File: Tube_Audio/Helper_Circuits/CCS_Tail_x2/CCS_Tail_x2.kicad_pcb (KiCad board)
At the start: 2 copper layers, 67.3 x 45.7 mm, 15 parts, among them J1 Screw_Terminal_01x03, Q1 IXCP10M45S, Q2 IXCP10M45S

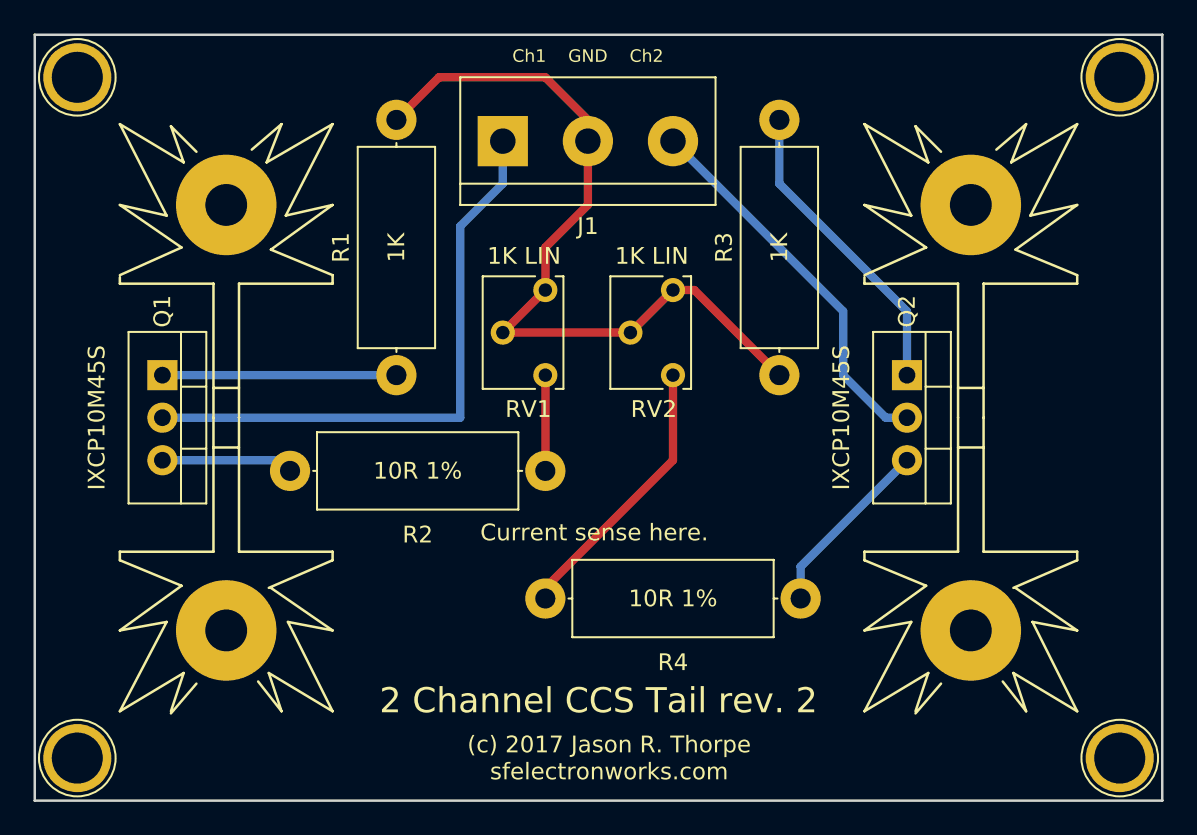
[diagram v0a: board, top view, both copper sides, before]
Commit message: Rev the CCS tail board -- use the Bourns 4-turn trim pots, and shrink the board a bit.
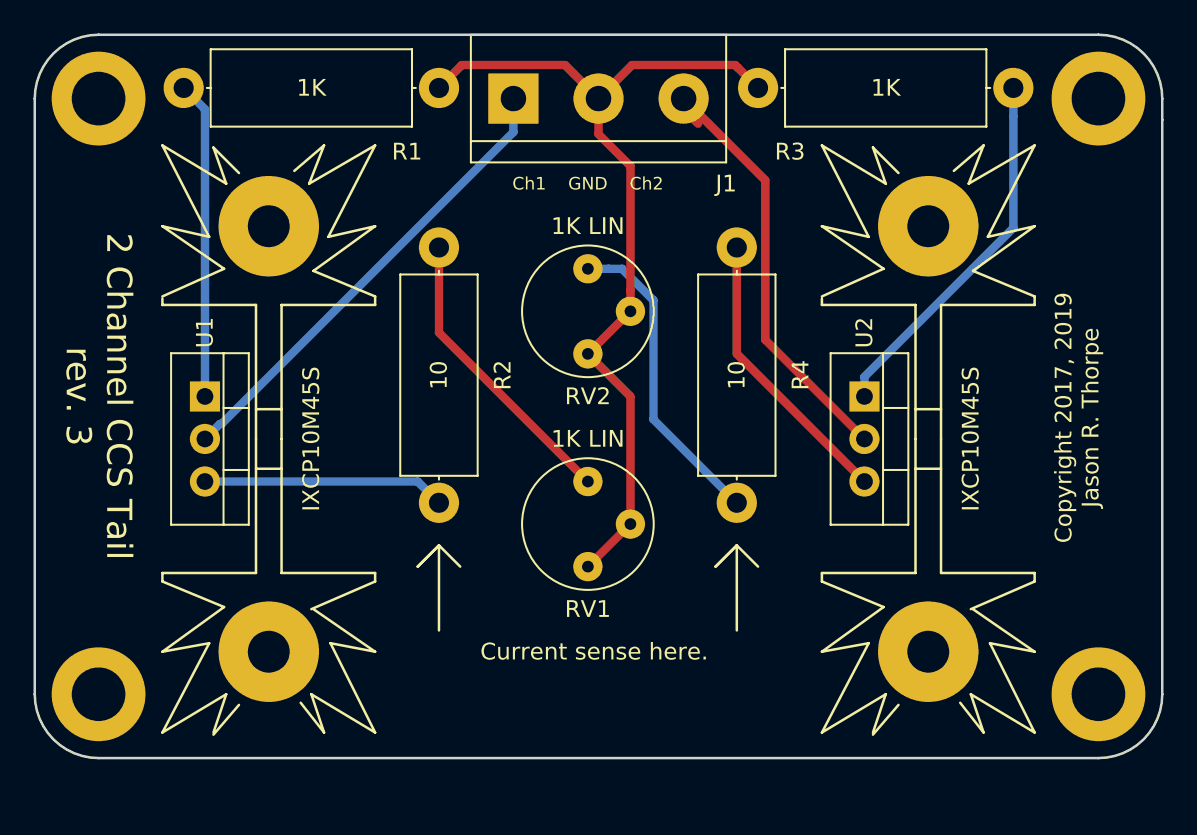
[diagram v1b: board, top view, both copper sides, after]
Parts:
- removed Screw (x4): 1pin, Connectors:1pin
- added REF**: MountingHole_3.2mm_M3_DIN965_Pad, MountingHole:MountingHole_3.2mm_M3_DIN965_Pad, F.Cu at (116.8, 129.5)
- added REF**: MountingHole_3.2mm_M3_DIN965_Pad, MountingHole:MountingHole_3.2mm_M3_DIN965_Pad, F.Cu at (176.5, 129.5)
- added REF**: MountingHole_3.2mm_M3_DIN965_Pad, MountingHole:MountingHole_3.2mm_M3_DIN965_Pad, F.Cu at (176.5, 94.0)
- added REF**: MountingHole_3.2mm_M3_DIN965_Pad, MountingHole:MountingHole_3.2mm_M3_DIN965_Pad, F.Cu at (116.8, 94.0)
- R2, R4: value 10R 1% -> 10
- RV1, RV2: footprint Potentiometers:Potentiometer_Trimmer_Vishay_T73XX_Vertical -> Potentiometer_THT:Potentiometer_Bourns_3339P_Vertical_HandSoldering
- moved R1 21.3 mm to (121.9, 93.3), turned to 0 degrees
- moved R4 21.3 mm to (154.9, 102.9), turned to 270 degrees
- moved R3 14.1 mm to (171.4, 93.3), turned to 180 degrees
- moved R2 9.09 mm to (137.2, 118.1), turned to 90 degrees
- moved RV2 8.13 mm to (146.1, 104.1)
- moved RV1 6.84 mm to (146.1, 116.8)
- moved Sink1 2.84 mm to (127.0, 114.3)
- moved U1 2.84 mm to (123.2, 111.8)
- moved U2 2.84 mm to (162.6, 111.8)
- moved Sink1 2.84 mm to (166.4, 114.3)
- moved J1 2.62 mm to (141.6, 94.0)
- renumbered Q1 to U1, Q2 to U2
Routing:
- net Net-(R2-Pad2): track 5.72 -> 17.7 mm
- net Net-(J1-Pad1): track 36.6 -> 28.0 mm
- net Net-(R2-Pad1): track 7.88 -> 14.5 mm
- net Net-(R4-Pad1): track 10.9 -> 17.1 mm
- net Net-(J1-Pad2): track 48.0 -> 53.7 mm
- net Net-(R1-Pad1): track 14.0 -> 18.9 mm
- net Net-(J1-Pad3): track 23.0 -> 26.9 mm
- net Net-(R3-Pad1): track 18.4 -> 22.1 mm
- net Net-(R4-Pad2): track 16.5 -> 18.8 mm
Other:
- board size 67.3 x 45.7 mm -> 67.3 x 43.2 mm
- net class Default: clearance 0.2 -> 0.25
- rule trace_clearance: 0.2 -> 0.25
- board text added: "2 Channel CCS Tail rev. 3"
- board text added: "Copyright 2017, 2019 Jason R. Thorpe"
- board text removed: "(c) 2017 Jason R. Thorpe sfelectronworks.com"
- board text removed: "2 Channel CCS Tail rev. 2"
